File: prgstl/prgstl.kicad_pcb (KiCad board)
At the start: 2 copper layers, 76.2 x 50.8 mm, 38 parts, among them J2 STM32WORLD_BASE, Q1 S9013, U1 AMS1117-3.3, U2 STM32F103CBTx, Y1 8MHz

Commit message: Hmmmm
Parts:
- C2: value 100nF -> C_100NF_0603; footprint Capacitor_SMD:C_0402_1005Metric -> Capacitor_SMD:C_0603_1608Metric
- R1: value 1K5 -> R_1.5K_0603; footprint Resistor_SMD:R_0402_1005Metric -> Resistor_SMD:R_0603_1608Metric
- R10, R2: value 100k -> R_100K_0603; footprint Resistor_SMD:R_0402_1005Metric -> Resistor_SMD:R_0603_1608Metric
- R11: value 100R -> R_100_0603; footprint Resistor_SMD:R_0402_1005Metric -> Resistor_SMD:R_0603_1608Metric
- R12, R8: value 10k -> R_10K_0603; footprint Resistor_SMD:R_0402_1005Metric -> Resistor_SMD:R_0603_1608Metric
- R17, R18: value 4k7 -> R_4.7K_0603; footprint Resistor_SMD:R_0402_1005Metric -> Resistor_SMD:R_0603_1608Metric
- R9: value 33k -> R_33K_0603; footprint Resistor_SMD:R_0402_1005Metric -> Resistor_SMD:R_0603_1608Metric
- Y1: value 8MHz -> X_8MHZ; footprint Crystal:Crystal_SMD_5032-2Pin_5.0x3.2mm -> stm32world:Crystal_SMD_5032-2Pin_5.0x3.2mm
- moved R10 17.6 mm to (150.5, 92.1)
- moved C2 12.1 mm to (145.4, 101.0)
- moved R2 10.0 mm to (145.4, 99.1), turned to 180 degrees
- moved R17 8.65 mm to (144.8, 105.4)
- moved R12 7.81 mm to (135.0, 111.1)
- moved R8 7.43 mm to (177.8, 90.8), turned to 0 degrees
- moved R1 5.85 mm to (172.1, 91.4)
- moved R11 5.68 mm to (165.7, 92.1)
- moved R18 3.36 mm to (144.1, 108.0), turned to 180 degrees
- moved R9 2.29 mm to (168.9, 94.6)
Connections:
- R1 pad 1: Net-(J1-PadA6) -> Net-(Q1-Pad2)
- R1 pad 2: Net-(Q1-Pad2) -> Net-(J1-PadA6)
- R10 pad 1: GND -> B0
- R10 pad 2: B0 -> GND
- R12 pad 1: GND -> Net-(R12-Pad1)
- R12 pad 2: Net-(R12-Pad2) -> GND
- R17 pad 1: Net-(R17-Pad1) -> +3V3
- R17 pad 2: +3V3 -> Net-(R17-Pad2)
- R18 pad 1: GND -> Net-(R17-Pad2)
- R18 pad 2: Net-(R17-Pad1) -> GND
- R2 pad 1: Net-(C2-Pad1) -> +3V3
- R2 pad 2: +3V3 -> Net-(C2-Pad1)
- R8 pad 1: Net-(Q1-Pad1) -> +5V
- R8 pad 2: +5V -> Net-(Q1-Pad1)
- R9 pad 1: GND -> Net-(Q1-Pad1)
- R9 pad 2: Net-(Q1-Pad1) -> GND
- U2 pad 10: Net-(R17-Pad1) -> Net-(R17-Pad2)
- U2 pad 2: Net-(R12-Pad2) -> Net-(R12-Pad1)
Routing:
- net Net-(C11-Pad1): track 0.52 -> 0.00 mm
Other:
- board text added: "PRGSTL, rev. a"

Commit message: Hmmm
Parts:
- removed the D3 at (125.1, 103.5)
- removed the R13 at (143.5, 94.0)
- added D2: LED_BLUE_0603, LED_SMD:LED_0603_1608Metric, F.Cu at (116.8, 93.3)
- added JP1: ~, Jumper:SolderJumper-2_P1.3mm_Bridged2Bar_Pad1.0x1.5mm, F.Cu at (121.9, 100.3)
- added JP2: ~, Jumper:SolderJumper-2_P1.3mm_Open_Pad1.0x1.5mm, F.Cu at (121.9, 102.9)
- added JP3: ~, Jumper:SolderJumper-2_P1.3mm_Open_Pad1.0x1.5mm, F.Cu at (121.9, 105.4)
- added JP4: ~, Jumper:SolderJumper-2_P1.3mm_Open_Pad1.0x1.5mm, F.Cu at (121.9, 108.0)
- added JP5: ~, Jumper:SolderJumper-2_P1.3mm_Bridged2Bar_Pad1.0x1.5mm, F.Cu at (132.1, 100.3)
- added JP6: ~, Jumper:SolderJumper-2_P1.3mm_Open_Pad1.0x1.5mm, F.Cu at (132.1, 102.9)
- added JP7: ~, Jumper:SolderJumper-2_P1.3mm_Open_Pad1.0x1.5mm, F.Cu at (132.1, 105.4)
- added JP8: ~, Jumper:SolderJumper-2_P1.3mm_Open_Pad1.0x1.5mm, F.Cu at (132.1, 108.0)
- added R15: DNP, Resistor_SMD:R_0603_1608Metric, F.Cu at (151.8, 94.6)
- moved R14 24.9 mm to (153.7, 94.6), turned to 90 degrees
- moved C2 13.6 mm to (169.5, 113.0), turned to 270 degrees
- moved R18 11.4 mm to (155.6, 108.6), turned to 270 degrees
- moved C5 11.3 mm to (151.8, 108.6), turned to 270 degrees
- moved R11 10.5 mm to (149.9, 108.6), turned to 90 degrees
- moved R12 10.2 mm to (175.9, 92.1), turned to 270 degrees
- moved R17 9.44 mm to (153.7, 108.6), turned to 90 degrees
- moved R8 9.25 mm to (177.8, 92.1), turned to 90 degrees
- moved C7 9.09 mm to (166.4, 106.7)
- moved C10 8.89 mm to (146.7, 102.9)
- moved Y1 8.89 mm to (149.9, 101.0)
- moved Q1 8.84 mm to (182.2, 92.1)
- moved R6 8.54 mm to (178.4, 97.2)
- moved C3 8.47 mm to (155.6, 94.6), turned to 90 degrees
- moved C8 8.03 mm to (148.0, 108.6), turned to 270 degrees
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- renumbered C11 to C10, C4 to C2, C5 to C3, C6 to C4, C7 to C5, C3 to C6, C8 to C7, C2 to C8, C10 to C9, D2 to D1, D4 to D3, D1 to D4, R7 to R1, R6 to R10, R2 to R11, R11 to R12, R10 to R13, R12 to R14, R14 to R16, R15 to R2, R16 to R3, R3 to R4, R4 to R5, R1 to R6, R8 to R7, R9 to R8, R5 to R9
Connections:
- J2 pad 11: Net-(J2-Pad11) -> USART2_TX
- J2 pad 12: Net-(J2-Pad12) -> USART2_RX
- J2 pad 23: Net-(J2-Pad23) -> USART3_TX
- J2 pad 24: Net-(J2-Pad24) -> USART3_RX
- J2 pad 4: Net-(J2-Pad4) -> T_RST
- J2 pad 50: Net-(J2-Pad50) -> USART1_TX
- J2 pad 51: Net-(J2-Pad51) -> USART1_RX
- J2 pad 54: Net-(J2-Pad54) -> T_DIO
- J2 pad 55: Net-(J2-Pad55) -> T_CLK
- J2 pad 64: Net-(J2-Pad64) -> T_SWO
- J2 pad 67: Net-(J2-Pad67) -> USART1_TX_ALT
- J2 pad 68: Net-(J2-Pad68) -> USART1_RX_ALT
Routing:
- net USART1_RX: track 0.00 -> 58.7 mm, vias 0 -> 1
- net USART1_TX: track 0.00 -> 54.4 mm, vias 0 -> 1
- net LED: track 0.00 -> 54.0 mm, vias 0 -> 2
- net T_RST: track 0.00 -> 47.9 mm
- net USART3_RX: track 0.00 -> 42.2 mm, vias 0 -> 1
- net T_TX: track 0.00 -> 41.7 mm, vias 0 -> 2
- net T_RX: track 0.00 -> 36.2 mm, vias 0 -> 2
- net T_SWO: track 0.00 -> 35.4 mm, vias 0 -> 1
- net USART2_RX: track 0.00 -> 33.1 mm
- net USART3_TX: track 0.00 -> 32.6 mm, vias 0 -> 1
- net USART1_RX_ALT: track 0.00 -> 32.6 mm, vias 0 -> 1
- net USART1_TX_ALT: track 0.00 -> 31.4 mm, vias 0 -> 1
- net T_DIO: track 0.00 -> 31.4 mm, vias 0 -> 1
- net T_CLK: track 0.00 -> 30.1 mm, vias 0 -> 1
- net USART2_TX: track 0.00 -> 21.3 mm
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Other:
- board text added: "USART1"
- board text added: "USART1_ALT"
- board text added: "USART2"
- board text added: "USART3"

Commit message: Added blank!
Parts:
- added U3: SRV05-4, Package_TO_SOT_SMD:SOT-23-6, F.Cu at (178.3, 102.1)
- moved R16 4.02 mm to (165.1, 108.6), turned to 270 degrees
- moved R10 3.81 mm to (174.6, 101.0)
- moved R4 3.81 mm to (174.6, 104.8)
- moved R5 3.81 mm to (174.6, 99.1)
- moved R6 3.81 mm to (174.6, 97.2)
- moved R9 3.81 mm to (174.6, 102.9)
- moved C7 3.70 mm to (163.2, 108.6), turned to 270 degrees
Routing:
- net T_DIO: track 31.4 -> 36.9 mm
- net Net-(J1-PadA7): track 6.48 -> 10.9 mm
- net Net-(J1-PadA6): track 9.72 -> 14.0 mm
- net Net-(J1-PadB5): track 3.71 -> 7.52 mm
- net Net-(J1-PadA5): track 4.18 -> 7.99 mm
- net D-: track 14.9 -> 11.1 mm
- net D+: track 14.3 -> 10.5 mm
- net Net-(Q1-Pad2): track 6.64 -> 9.27 mm
- net Net-(R16-Pad1): track 2.17 -> 4.05 mm
- net +3V3: track 244.2 -> 245.1 mm, vias 14 -> 15
- net GND: vias 22 -> 20

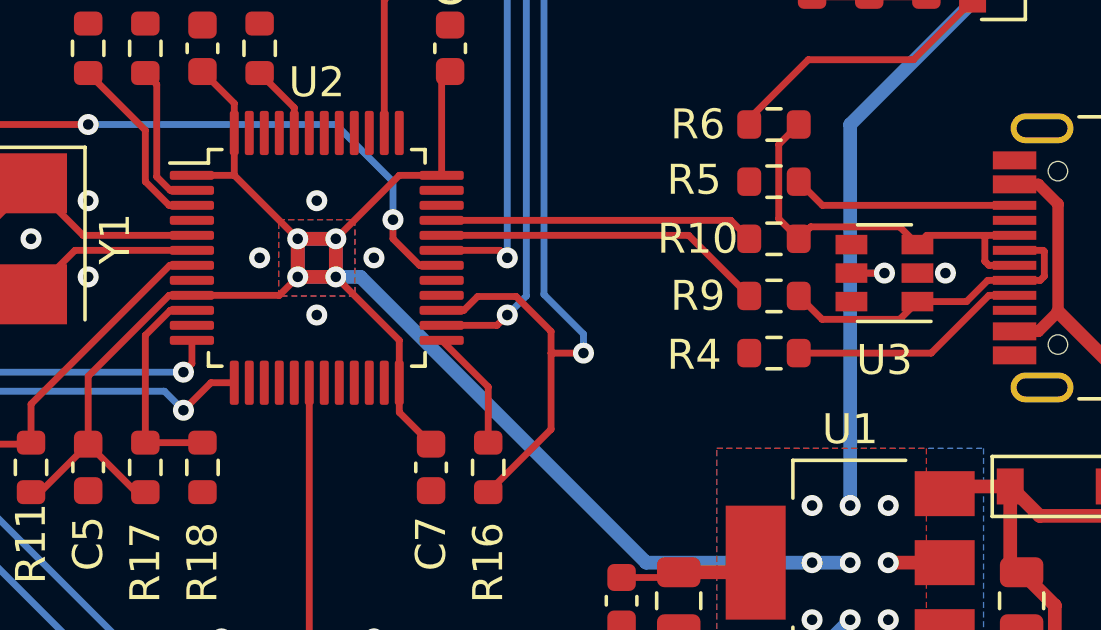
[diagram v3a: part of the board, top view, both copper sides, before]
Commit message: Added SPI Flash Module MEMW25Q128
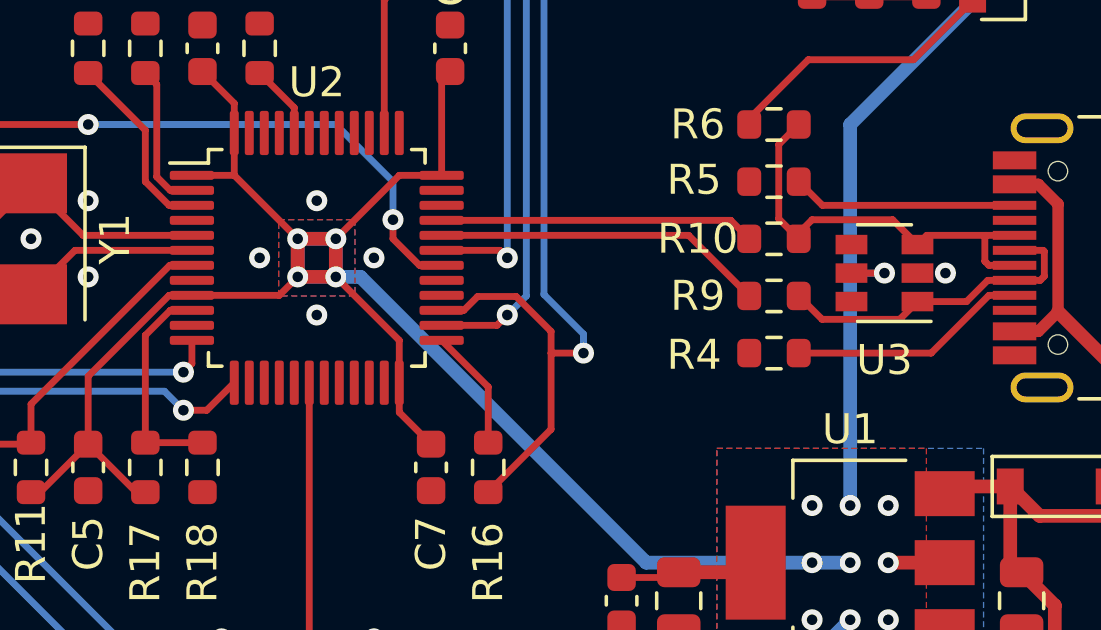
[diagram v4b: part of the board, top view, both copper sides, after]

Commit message: Hmmm
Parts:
- added JP10: ~, Jumper:SolderJumper-2_P1.3mm_Open_Pad1.0x1.5mm, F.Cu at (167.6, 95.2)
- added JP9: ~, Jumper:SolderJumper-2_P1.3mm_Open_Pad1.0x1.5mm, F.Cu at (167.6, 92.7)
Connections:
- J2 pad 45: Net-(J2-Pad45) -> P_CLK
- J2 pad 46: Net-(J2-Pad46) -> P_DIO
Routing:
- net P_DIO: track 0.00 -> 13.5 mm, vias 0 -> 1
- net P_CLK: track 0.00 -> 13.5 mm, vias 0 -> 1
- net CLK: track 0.00 -> 8.61 mm
- net DIO: track 0.00 -> 7.22 mm
- net GND: vias 20 -> 21

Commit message: Hmmmm
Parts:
- moved Q1 0.63 mm to (182.9, 92.1)
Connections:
- J1 pad A8: Net-(J1-PadA8) -> unconnected-(J1-PadA8)
- J1 pad B8: Net-(J1-PadB8) -> unconnected-(J1-PadB8)
- J2 pad 10: Net-(J2-Pad10) -> unconnected-(J2-Pad10)
- J2 pad 13: Net-(J2-Pad13) -> unconnected-(J2-Pad13)
- J2 pad 14: Net-(J2-Pad14) -> unconnected-(J2-Pad14)
- J2 pad 15: Net-(J2-Pad15) -> unconnected-(J2-Pad15)
- J2 pad 16: Net-(J2-Pad16) -> unconnected-(J2-Pad16)
- J2 pad 17: Net-(J2-Pad17) -> unconnected-(J2-Pad17)
- J2 pad 18: Net-(J2-Pad18) -> unconnected-(J2-Pad18)
- J2 pad 19: Net-(J2-Pad19) -> unconnected-(J2-Pad19)
- J2 pad 20: Net-(J2-Pad20) -> unconnected-(J2-Pad20)
- J2 pad 21: Net-(J2-Pad21) -> unconnected-(J2-Pad21)
- J2 pad 22: Net-(J2-Pad22) -> unconnected-(J2-Pad22)
- J2 pad 25: Net-(J2-Pad25) -> unconnected-(J2-Pad25)
- J2 pad 26: Net-(J2-Pad26) -> unconnected-(J2-Pad26)
- J2 pad 27: Net-(J2-Pad27) -> unconnected-(J2-Pad27)
- J2 pad 28: Net-(J2-Pad28) -> unconnected-(J2-Pad28)
- J2 pad 29: Net-(J2-Pad29) -> unconnected-(J2-Pad29)
- J2 pad 3: Net-(J2-Pad3) -> unconnected-(J2-Pad3)
- J2 pad 30: Net-(J2-Pad30) -> unconnected-(J2-Pad30)
- J2 pad 31: Net-(J2-Pad31) -> unconnected-(J2-Pad31)
- J2 pad 32: Net-(J2-Pad32) -> unconnected-(J2-Pad32)
- J2 pad 33: Net-(J2-Pad33) -> unconnected-(J2-Pad33)
- J2 pad 34: Net-(J2-Pad34) -> unconnected-(J2-Pad34)
- J2 pad 35: Net-(J2-Pad35) -> unconnected-(J2-Pad35)
- J2 pad 36: Net-(J2-Pad36) -> unconnected-(J2-Pad36)
- J2 pad 47: Net-(J2-Pad47) -> unconnected-(J2-Pad47)
- J2 pad 48: Net-(J2-Pad48) -> unconnected-(J2-Pad48)
- J2 pad 49: Net-(J2-Pad49) -> unconnected-(J2-Pad49)
- J2 pad 5: Net-(J2-Pad5) -> unconnected-(J2-Pad5)
- J2 pad 52: Net-(J2-Pad52) -> unconnected-(J2-Pad52)
- J2 pad 53: Net-(J2-Pad53) -> unconnected-(J2-Pad53)
- J2 pad 56: Net-(J2-Pad56) -> unconnected-(J2-Pad56)
- J2 pad 57: Net-(J2-Pad57) -> unconnected-(J2-Pad57)
- J2 pad 58: Net-(J2-Pad58) -> unconnected-(J2-Pad58)
- J2 pad 59: Net-(J2-Pad59) -> unconnected-(J2-Pad59)
- J2 pad 6: Net-(J2-Pad6) -> unconnected-(J2-Pad6)
- J2 pad 60: Net-(J2-Pad60) -> unconnected-(J2-Pad60)
- J2 pad 61: Net-(J2-Pad61) -> unconnected-(J2-Pad61)
- J2 pad 62: Net-(J2-Pad62) -> unconnected-(J2-Pad62)
- J2 pad 63: Net-(J2-Pad63) -> unconnected-(J2-Pad63)
- J2 pad 65: Net-(J2-Pad65) -> unconnected-(J2-Pad65)
- J2 pad 66: Net-(J2-Pad66) -> unconnected-(J2-Pad66)
- J2 pad 69: Net-(J2-Pad69) -> unconnected-(J2-Pad69)
- J2 pad 7: Net-(J2-Pad7) -> unconnected-(J2-Pad7)
- J2 pad 70: Net-(J2-Pad70) -> unconnected-(J2-Pad70)
- J2 pad 71: Net-(J2-Pad71) -> unconnected-(J2-Pad71)
- J2 pad 72: Net-(J2-Pad72) -> unconnected-(J2-Pad72)
- J2 pad 73: Net-(J2-Pad73) -> unconnected-(J2-Pad73)
- J2 pad 74: Net-(J2-Pad74) -> unconnected-(J2-Pad74)
- J2 pad 75: Net-(J2-Pad75) -> unconnected-(J2-Pad75)
- J2 pad 76: Net-(J2-Pad76) -> unconnected-(J2-Pad76)
- J2 pad 77: Net-(J2-Pad77) -> unconnected-(J2-Pad77)
- J2 pad 78: Net-(J2-Pad78) -> unconnected-(J2-Pad78)
- J2 pad 8: Net-(J2-Pad8) -> unconnected-(J2-Pad8)
- J2 pad 9: Net-(J2-Pad9) -> unconnected-(J2-Pad9)
- U2 pad 11: Net-(U2-Pad11) -> unconnected-(U2-Pad11)
- U2 pad 14: Net-(U2-Pad14) -> unconnected-(U2-Pad14)
- U2 pad 15: Net-(U2-Pad15) -> unconnected-(U2-Pad15)
- U2 pad 16: Net-(U2-Pad16) -> unconnected-(U2-Pad16)
- U2 pad 17: Net-(U2-Pad17) -> unconnected-(U2-Pad17)
- U2 pad 19: Net-(U2-Pad19) -> unconnected-(U2-Pad19)
- U2 pad 20: Net-(U2-Pad20) -> unconnected-(U2-Pad20)
- U2 pad 21: Net-(U2-Pad21) -> unconnected-(U2-Pad21)
- U2 pad 22: Net-(U2-Pad22) -> unconnected-(U2-Pad22)
- U2 pad 28: Net-(U2-Pad28) -> unconnected-(U2-Pad28)
- U2 pad 29: Net-(U2-Pad29) -> unconnected-(U2-Pad29)
- U2 pad 39: Net-(U2-Pad39) -> unconnected-(U2-Pad39)
- U2 pad 4: Net-(U2-Pad4) -> unconnected-(U2-Pad4)
- U2 pad 40: Net-(U2-Pad40) -> unconnected-(U2-Pad40)
- U2 pad 41: Net-(U2-Pad41) -> unconnected-(U2-Pad41)
- U2 pad 42: Net-(U2-Pad42) -> unconnected-(U2-Pad42)
- U2 pad 43: Net-(U2-Pad43) -> unconnected-(U2-Pad43)
- U2 pad 45: Net-(U2-Pad45) -> unconnected-(U2-Pad45)
- U2 pad 46: Net-(U2-Pad46) -> unconnected-(U2-Pad46)
- U3 pad 4: Net-(U3-Pad4) -> unconnected-(U3-Pad4)
- U3 pad 6: Net-(U3-Pad6) -> unconnected-(U3-Pad6)
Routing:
- net VBUS: track 13.6 -> 17.7 mm
- net Net-(Q1-Pad2): track 9.27 -> 9.97 mm
- net Net-(Q1-Pad1): track 6.22 -> 6.78 mm
- net GND: vias 21 -> 31
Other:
- net class Default removed

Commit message: Hmmm
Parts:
- moved D1 1.27 mm to (118.1, 89.5)
- moved D2 1.27 mm to (118.1, 93.3)
- moved D3 1.27 mm to (118.1, 91.4)
- moved R1 1.27 mm to (121.3, 89.5)
- moved R2 1.27 mm to (121.3, 93.3)
- moved R3 1.27 mm to (121.3, 91.4)
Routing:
- net +3V3: track 245.3 -> 243.1 mm
- net USART1_TX: track 54.4 -> 53.1 mm
- net Net-(C10-Pad1): track 9.44 -> 8.42 mm
- net LED: track 54.0 -> 53.5 mm
